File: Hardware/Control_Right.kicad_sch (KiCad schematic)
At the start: 0 parts

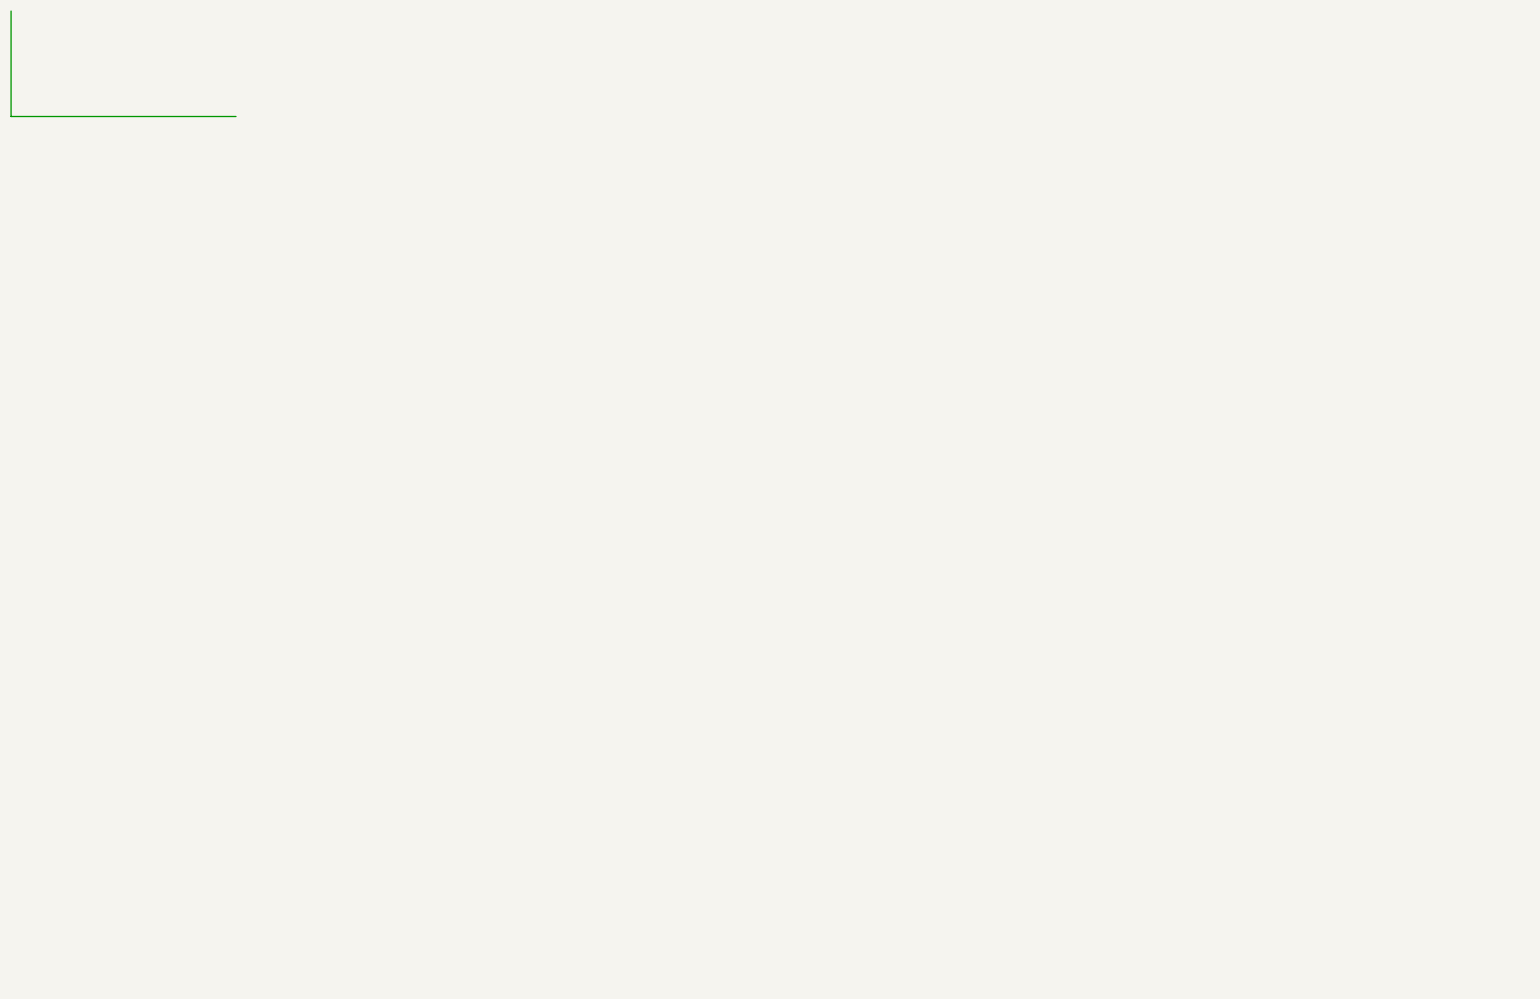
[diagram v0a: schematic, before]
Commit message: Schematic review
Initial shcematic iteration.
Added all footprints and part numbers.
Only a quick review was performed.
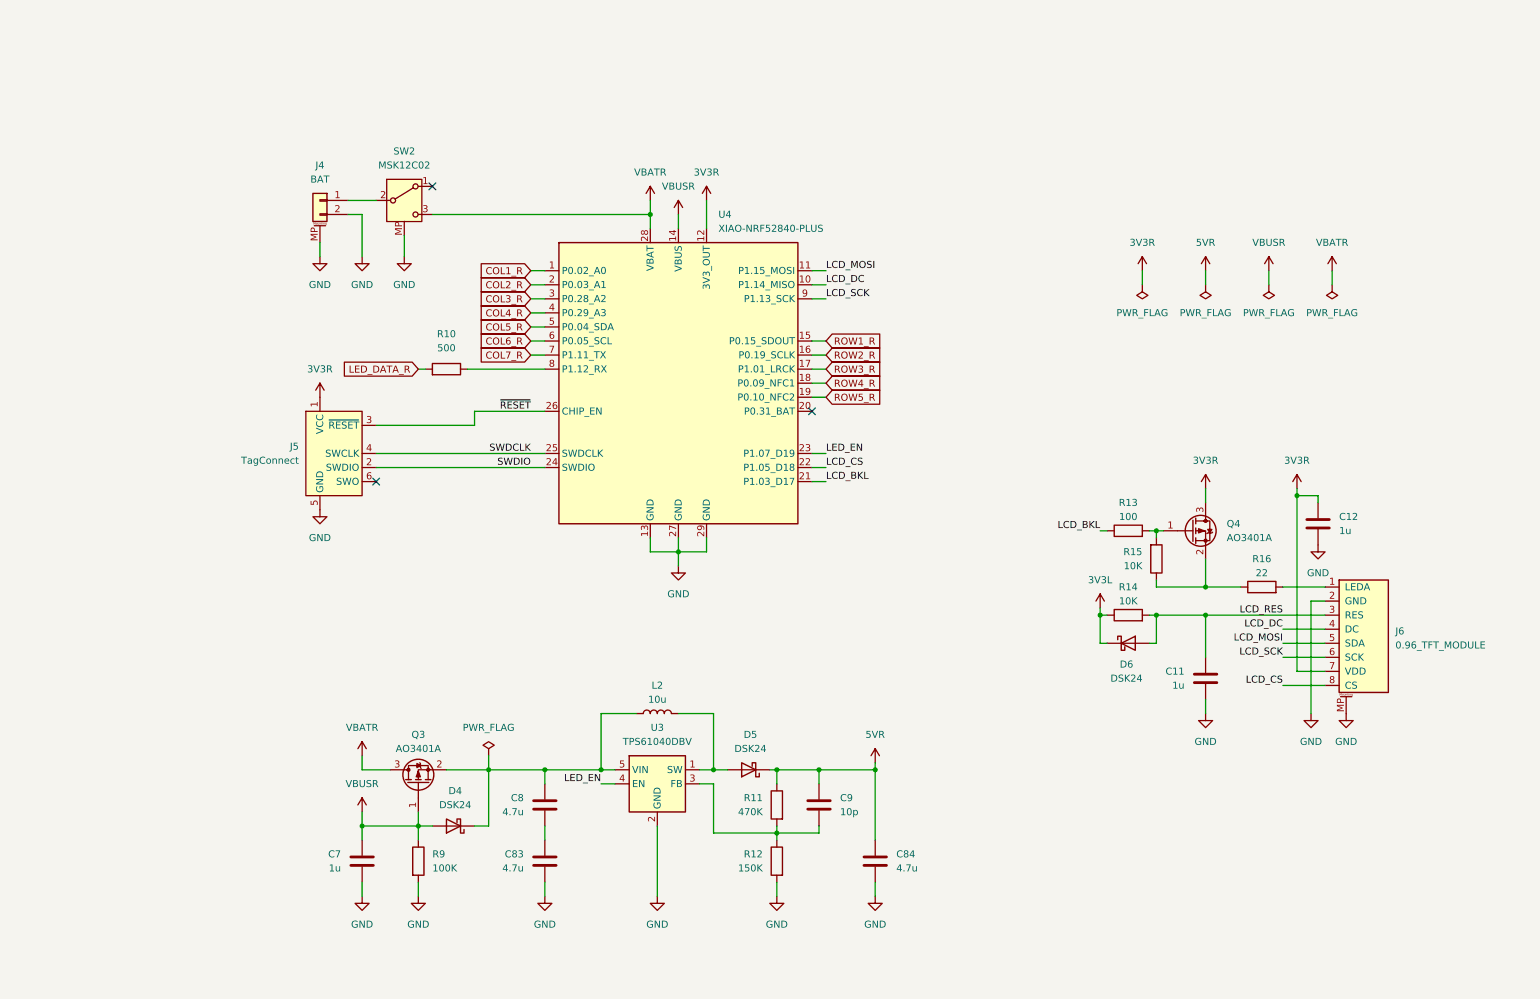
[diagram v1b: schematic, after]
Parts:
- added C11, C12, C7: 1u, Capacitor_SMD:C_0603_1608Metric, symbol Device:C
- added C8, C83, C84: 4.7u, Capacitor_SMD:C_1206_3216Metric, symbol Device:C
- added C9: 10p, Capacitor_SMD:C_0603_1608Metric, symbol Device:C
- added D4, D5, D6: DSK24, Diode_SMD:D_SOD-123F, symbol Device:D_Schottky
- added J4: BAT, Custom_Parts:JST_PH_1x02_P2.00MM_SMD_HOR, symbol Connector_Generic_MountingPin:Conn_01x02_MountingPin
- added J5: TagConnect, Connector:Tag-Connect_TC2030-IDC-NL_2x03_P1.27mm_Vertical, symbol Connector:Conn_ARM_SWD_TagConnect_TC2030-NL
- added J6: 0.96_TFT_MODULE, Custom_Parts:Jushuo_AFC07-S06FCA-00_1x8-1MP_P0.50_Horizontal, symbol Custom_Parts:0.96_TFT_MODULE
- added L2: 10u, Custom_Parts:VLCF4020, symbol Device:L
- added Q3, Q4: AO3401A, Package_TO_SOT_SMD:SOT-23, symbol Transistor_FET:AO3401A
- added R10: 500, Resistor_SMD:R_0603_1608Metric, symbol Device:R
- added R11: 470K, Resistor_SMD:R_0603_1608Metric, symbol Device:R
- added R12: 150K, Resistor_SMD:R_0603_1608Metric, symbol Device:R
- added R13: 100, Resistor_SMD:R_0603_1608Metric, symbol Device:R
- added R14, R15: 10K, Resistor_SMD:R_0603_1608Metric, symbol Device:R
- added R16: 22, Resistor_SMD:R_0603_1608Metric, symbol Device:R
- added R9: 100K, Resistor_SMD:R_0603_1608Metric, symbol Device:R
- added SW2: MSK12C02, Custom_Parts:MSK12C02, symbol Custom_Parts:MSK12C02
- added U3: TPS61040DBV, Package_TO_SOT_SMD:SOT-23-5, symbol Regulator_Switching:TPS61040DBV
- added U4: XIAO-NRF52840-PLUS, Custom_Parts:XIAO-NRF52840-PLUS-SMD, symbol Custom_Parts:XIAO-NRF52840-PLUS-SMD
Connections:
- new net: R10.1, U4.8 (P1.12_RX)
- new net: J4.1 (Pin_1), SW2.2 (B)
- new net: D5.2 (A), L2.2, U3.1 (SW)
- new net: C9.2, R11.2, R12.1, U3.3 (FB)
- new net: C8.1, D4.1 (K), L2.1, Q3.2 (S), U3.5 (VIN)
- new net: C8.2, C83.1
- new net: J6.1 (LEDA), R16.2
- new net: Q4.1 (G), R13.2, R15.2
- new net: Q4.2 (S), R15.1, R16.1
- new net 3V3L: D6.1 (K), R14.1
- new net 3V3R: C12.1, J5.1 (VCC), J6.7 (VDD), Q4.3 (D), U4.12 (3V3_OUT)
- new net 5VR: C84.1, C9.1, D5.1 (K), R11.1
- new net COL1_R: U4.1 (P0.02_A0)
- new net COL2_R: U4.2 (P0.03_A1)
- new net COL3_R: U4.3 (P0.28_A2)
- new net COL4_R: U4.4 (P0.29_A3)
- new net COL5_R: U4.5 (P0.04_SDA)
- new net COL6_R: U4.6 (P0.05_SCL)
- new net COL7_R: U4.7 (P1.11_TX)
- new net GND: C11.2, C12.2, C7.2, C83.2, C84.2, J4.2 (Pin_2), J4.MP (MountPin), J5.5 (GND), J6.2 (GND), J6.MP, R12.2, R9.2, SW2.MP, U3.2 (GND), U4.13 (GND), U4.27 (GND), U4.29 (GND)
- new net LCD_BKL: R13.1, U4.21 (P1.03_D17)
- new net LCD_CS: J6.8 (CS), U4.22 (P1.05_D18)
- new net LCD_DC: J6.4 (DC), U4.10 (P1.14_MISO)
- new net LCD_MOSI: J6.5 (SDA), U4.11 (P1.15_MOSI)
- new net LCD_RES: C11.1, D6.2 (A), J6.3 (RES), R14.2
- new net LCD_SCK: J6.6 (SCK), U4.9 (P1.13_SCK)
- new net LED_DATA_R: R10.2
- new net LED_EN: U3.4 (EN), U4.23 (P1.07_D19)
- new net ROW1_R: U4.15 (P0.15_SDOUT)
- new net ROW2_R: U4.16 (P0.19_SCLK)
- new net ROW3_R: U4.17 (P1.01_LRCK)
- new net ROW4_R: U4.18 (P0.09_NFC1)
- new net ROW5_R: U4.19 (P0.10_NFC2)
- new net SWDCLK: J5.4 (SWCLK), U4.25 (SWDCLK)
- new net SWDIO: J5.2 (SWDIO), U4.24 (SWDIO)
- new net VBATR: Q3.3 (D), SW2.3 (C), U4.28 (VBAT)
- new net VBUSR: C7.1, D4.2 (A), Q3.1 (G), R9.1, U4.14 (VBUS)
- new net ~{RESET}: J5.3 (~{RESET}), U4.26 (CHIP_EN)
- no-connect marks 0 -> 3

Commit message: Net configurations
Added net labels.
Updated the PCB components.
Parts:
- removed C8: 4.7u, Capacitor_SMD:C_1206_3216Metric, symbol Device:C
- renumbered C84 to C10, C83 to C8, R9 to R10, R10 to R9
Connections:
- net LED_DATA: now reaches R9.1, U4.8 (P1.12_RX)
- net VBAT: now reaches J4.1 (Pin_1), SW2.2 (B)
- net VSWR: now reaches D5.2 (A), L2.2, U3.1 (SW)
- net VFBR: now reaches C9.2, R11.2, R12.1, U3.3 (FB)
- net VREGR: now reaches D4.1 (K), L2.1, Q3.2 (S), U3.5 (VIN)
- net VREGR: now also C8.1
- net BKL: now reaches J6.1 (LEDA), R16.2
- net BKLG: now reaches Q4.1 (G), R13.2, R15.2
- net BKLD: now reaches Q4.2 (S), R15.1, R16.1
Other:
- moved on the sheet: R13, R16, R9

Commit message: Initial layout
Configured the switch and LED initial layout.
Need to add the capacitors for the LEDs and the diodes for the switches.
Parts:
- added R12: 10K, Resistor_SMD:R_0603_1608Metric, symbol Device:R
- renumbered R9 to R10, R10 to R11, R11 to R13, R12 to R14, R13 to R15, R14 to R16, R15 to R17, R16 to R18
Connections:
- net COL7_R is gone; now on net LED_EN: U4.7 (P1.11_TX)
- net GND: now also R12.1
- net LED_EN: now also R12.2; no longer U4.23 (P1.07_D19)
- new net ROW6_R: U4.23 (P1.07_D19)

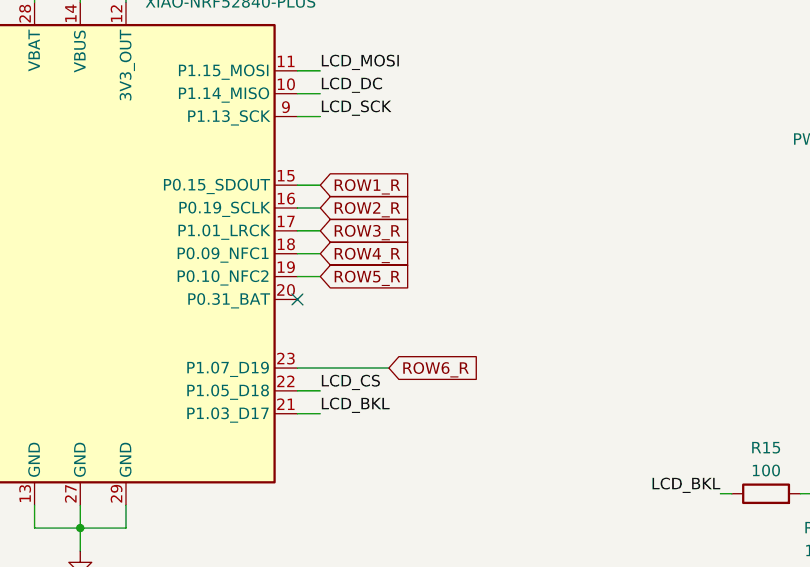
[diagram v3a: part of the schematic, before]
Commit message: Pin adjustment
Adjusted the pins for the encoders and other.
Now the battery measuring pin connected to an internal ADC on the XIAO nRF52840 also serves to read the rotation of the encoders.
Attention should be put as how to implement the BAT voltage measuring to check if the encoder is turning at the same time.
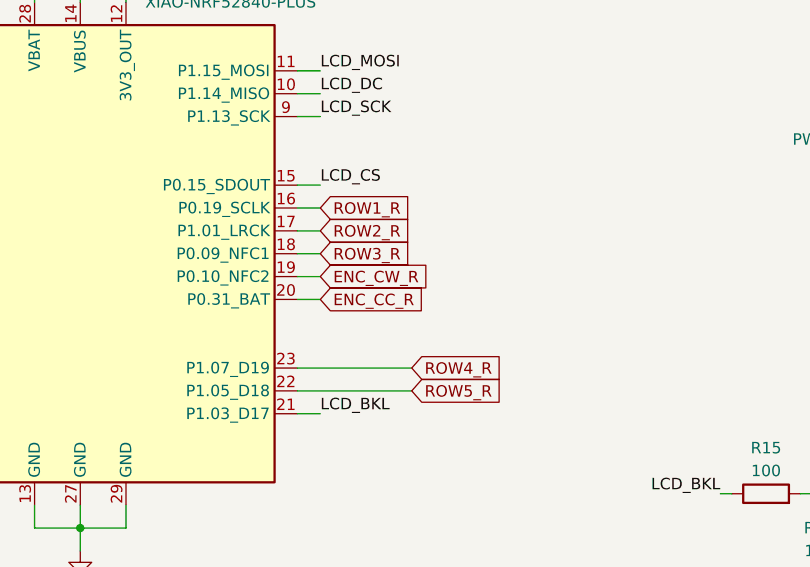
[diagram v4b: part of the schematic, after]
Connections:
- net ROW6_R is gone; now on net ROW4_R: U4.23 (P1.07_D19)
- net LCD_CS: now also U4.15 (P0.15_SDOUT); no longer U4.22 (P1.05_D18)
- net ROW1_R: now also U4.16 (P0.19_SCLK); no longer U4.15 (P0.15_SDOUT)
- net ROW2_R: now also U4.17 (P1.01_LRCK); no longer U4.16 (P0.19_SCLK)
- net ROW3_R: now also U4.18 (P0.09_NFC1); no longer U4.17 (P1.01_LRCK)
- net ROW4_R: no longer U4.18 (P0.09_NFC1)
- net ROW5_R: now also U4.22 (P1.05_D18); no longer U4.19 (P0.10_NFC2)
- net ENC_CC_R: now reaches U4.20 (P0.31_BAT)
- new net ENC_CW_R: U4.19 (P0.10_NFC2)
- no-connect marks 3 -> 2

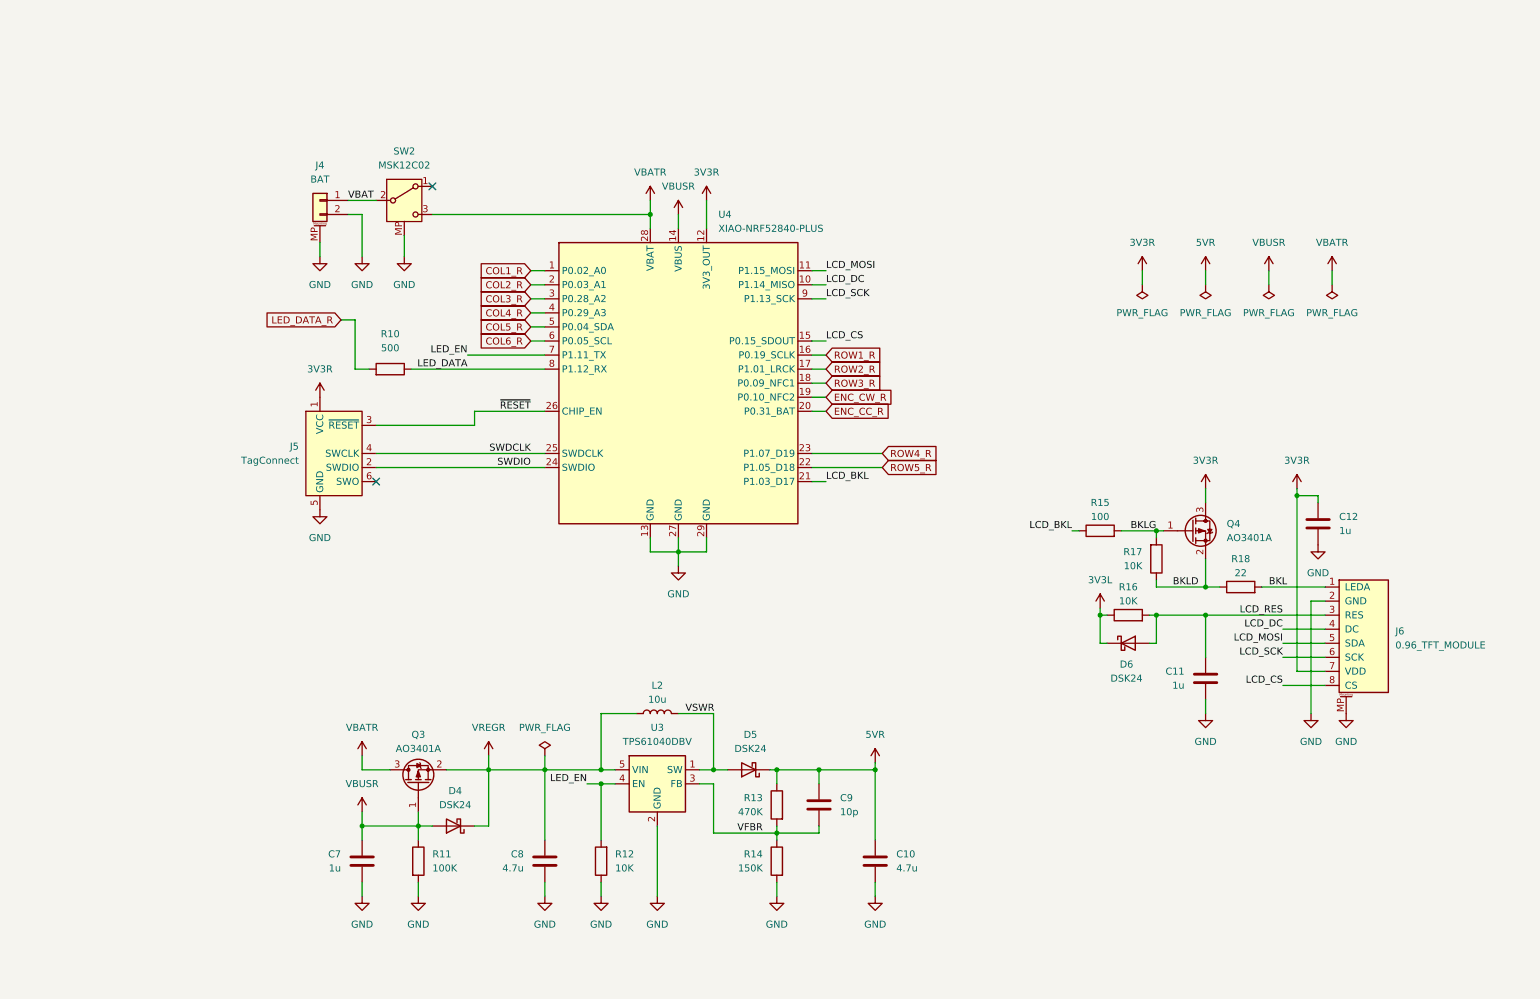
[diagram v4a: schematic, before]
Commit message: Key matrix and edges
Defined the key matrix locations and the board edges.
Next step: start routing and verify the buck converter layout.
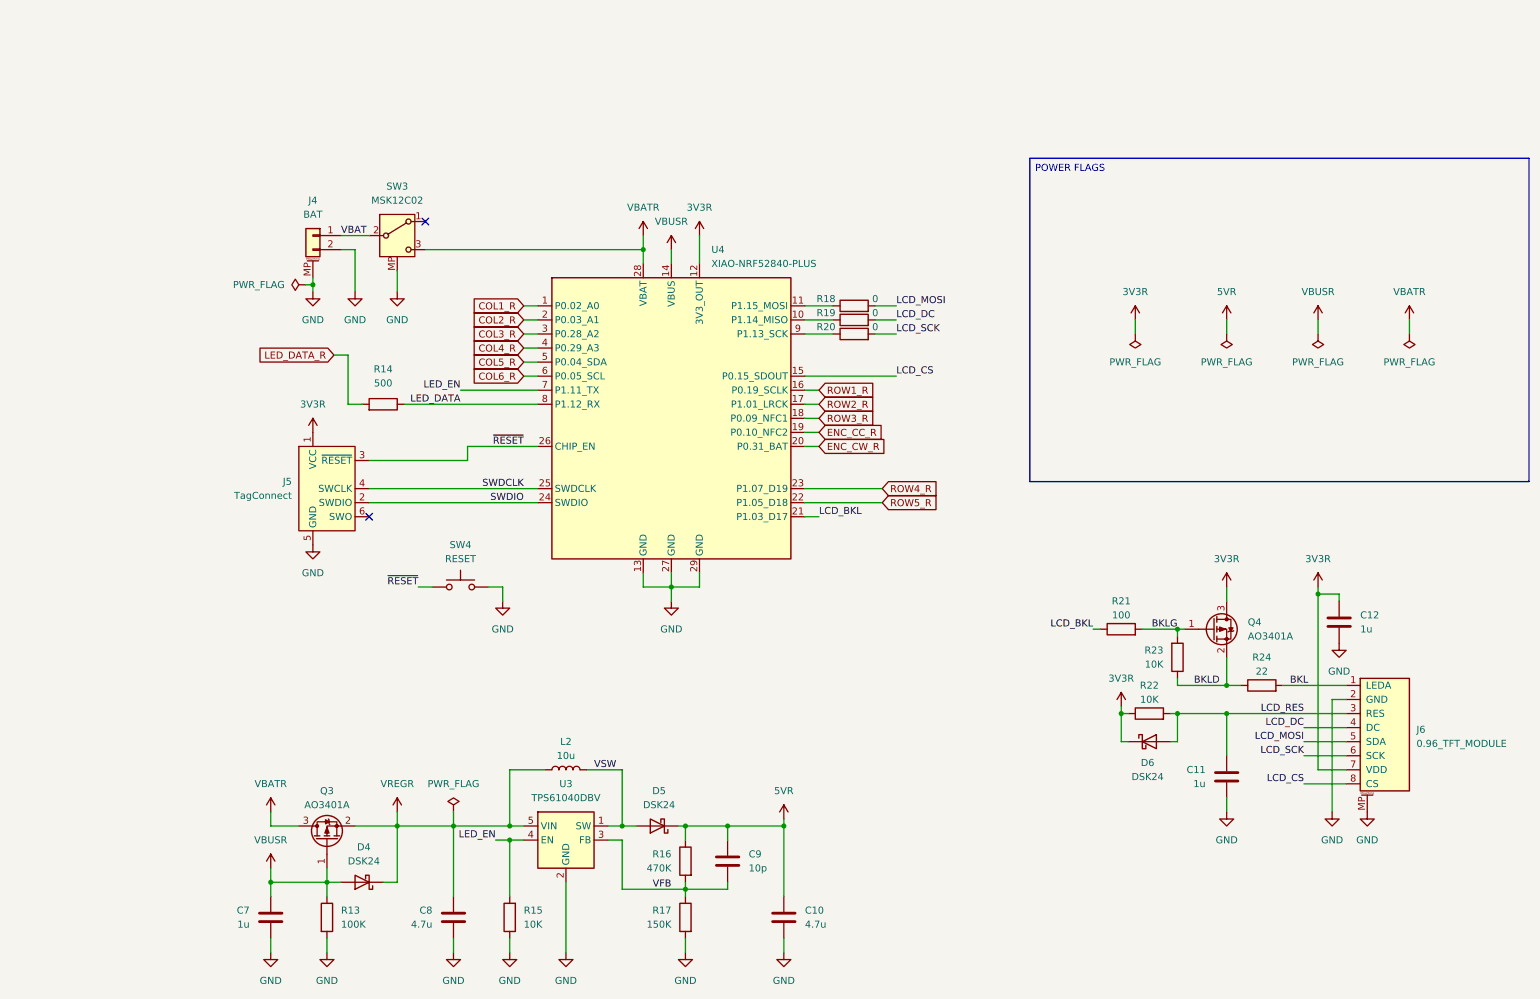
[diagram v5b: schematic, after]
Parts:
- removed R11: 100K, Resistor_SMD:R_0603_1608Metric, symbol Device:R
- removed R12: 10K, Resistor_SMD:R_0603_1608Metric, symbol Device:R
- removed R14: 150K, Resistor_SMD:R_0603_1608Metric, symbol Device:R
- added R19, R20: 0, Resistor_SMD:R_0603_1608Metric, symbol Device:R
- added R21: 100, Resistor_SMD:R_0603_1608Metric, symbol Device:R
- added R22, R23: 10K, Resistor_SMD:R_0603_1608Metric, symbol Device:R
- added R24: 22, Resistor_SMD:R_0603_1608Metric, symbol Device:R
- added SW4: RESET, Button_Switch_SMD:SW_SPST_TS-1088-xR020, symbol Switch:SW_Push
- J6: footprint Custom_Parts:Jushuo_AFC07-S06FCA-00_1x8-1MP_P0.50_Horizontal -> Custom_Parts:0.96_TFT_MODULE
- L2: footprint Custom_Parts:VLCF4020 -> Custom_Parts:VLCF4020_MIRROR
- R13: value 470K -> 100K; JLC Part C23178 -> C25803; Manufacturer Part 0603WAF4703T5E -> 0603WAF1003T5E
- R15: value 100 -> 10K; JLC Part 0603WAF1000T5E -> 0603WAF1002T5E; Manufacturer Part 0603WAF1000T5E -> 0603WAF1002T5E
- R16: value 10K -> 470K; JLC Part 0603WAF1002T5E -> C23178; Manufacturer Part 0603WAF1002T5E -> 0603WAF4703T5E
- R17: value 10K -> 150K; JLC Part 0603WAF1002T5E -> C22807; Manufacturer Part 0603WAF1002T5E -> 0603WAF1503T5E
- R18: value 22 -> 0; JLC Part C23345 -> C21189; Manufacturer Part 0603WAF220JT5E -> 0603WAF0000T5E
- renumbered R10 to R14, SW2 to SW3
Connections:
- net 3V3R: now also D6.1 (K), R22.1
- net 5VR: now also R16.1; no longer R13.1
- net BKL: now also R24.2; no longer R18.2
- net BKLD: now also R23.1, R24.1; no longer R17.1, R18.1
- net BKLG: now also R21.2, R23.2; no longer R15.2, R17.2
- net ENC_CC_R: now also U4.19 (P0.10_NFC2); no longer U4.20 (P0.31_BAT)
- net ENC_CW_R: now also U4.20 (P0.31_BAT); no longer U4.19 (P0.10_NFC2)
- net GND: now also R13.2, R15.1, R17.2, SW4.2
- net LCD_BKL: now also R21.1; no longer R15.1
- net LCD_DC: now also R19.2; no longer U4.10 (P1.14_MISO)
- net LCD_MOSI: now also R18.2; no longer U4.11 (P1.15_MOSI)
- net LCD_RES: now also R22.2; no longer R16.2
- net LCD_SCK: now also R20.2; no longer U4.9 (P1.13_SCK)
- net LED_EN: now also R15.2
- net VBUSR: now also R13.1
- net ~{RESET}: now also SW4.1
- removed net 3V3L: D6.1 (K), R16.1
- net VFBR renamed VFB
- net VFB: now also R16.2, R17.1; no longer R13.2
- net VSWR renamed VSW
- new net: R19.1, U4.10 (P1.14_MISO)
- new net: R18.1, U4.11 (P1.15_MOSI)
- new net: R20.1, U4.9 (P1.13_SCK)
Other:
- moved on the sheet: J4, J5, R14, SW3, U4
